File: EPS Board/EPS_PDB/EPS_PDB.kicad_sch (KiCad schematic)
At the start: 17 parts, among them J1 USB_B_Micro, J2 Conn_01x04_Pin, J3 Conn_02x26_Odd_Even, J4 Conn_02x26_Odd_Even, U1 AMS1117-3.3

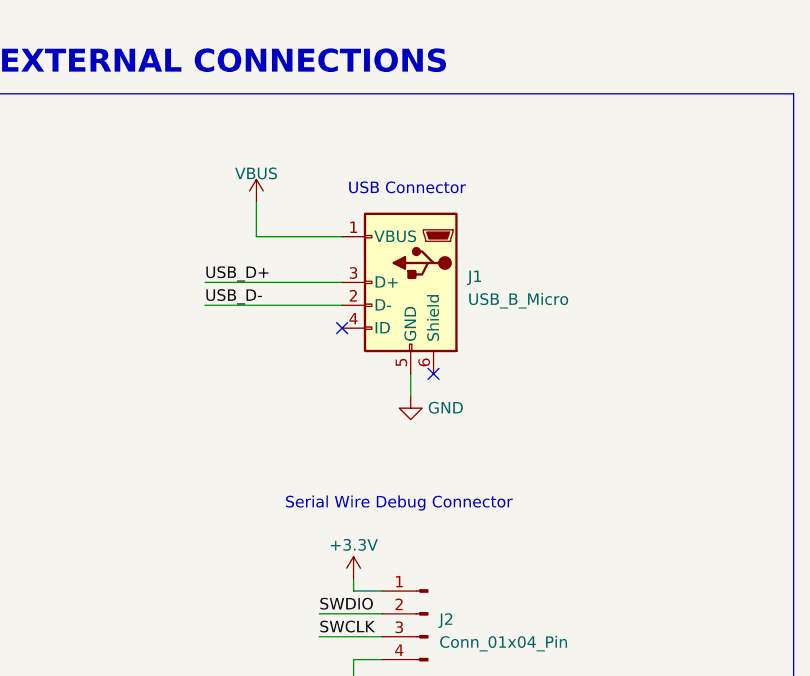
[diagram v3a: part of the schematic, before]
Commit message: texts added in schematics for clarity
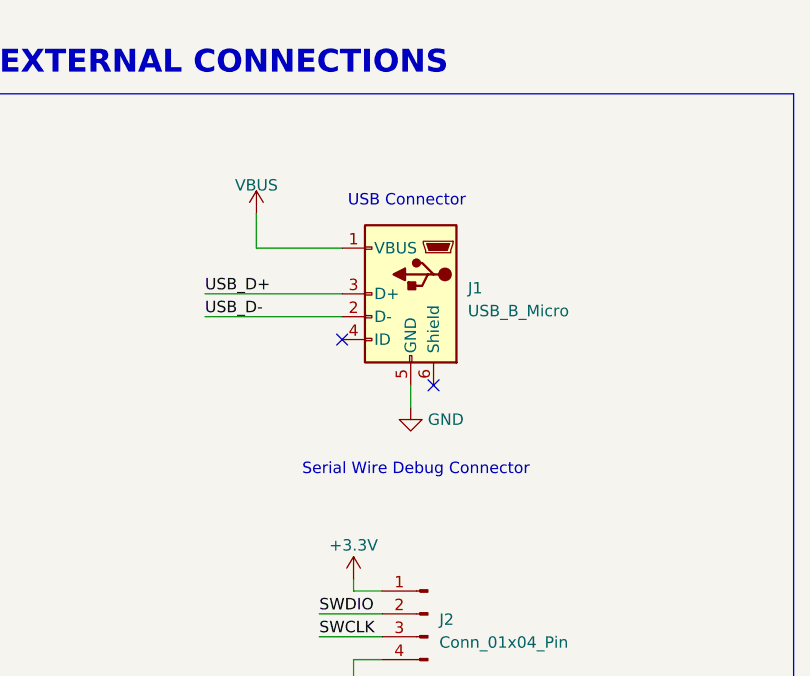
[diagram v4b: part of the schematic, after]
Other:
- moved on the sheet: J1
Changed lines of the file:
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@@
 	)
 	(no_connect
-		(at 216.535 116.84)
+		(at 216.535 118.11)
 	)
 	(no_connect
@@
 	)
 	(no_connect
-		(at 226.695 121.92)
+		(at 226.695 123.19)
 	)
 	(no_connect
@@
 	(wire
 		(pts
-			(xy 201.295 111.76) (xy 216.535 111.76)
+			(xy 201.295 113.03) (xy 216.535 113.03)
 		)
 		(stroke
@@
 	(wire
 		(pts
-			(xy 207.01 102.87) (xy 207.01 106.68)
+			(xy 207.01 104.14) (xy 207.01 107.95)
 		)
 		(stroke
@@
 	(wire
 		(pts
-			(xy 201.295 114.3) (xy 216.535 114.3)
+			(xy 201.295 115.57) (xy 216.535 115.57)
 		)
 		(stroke
@@
 	(wire
 		(pts
-			(xy 224.155 121.92) (xy 224.155 124.46)
+			(xy 224.155 123.19) (xy 224.155 125.73)
 		)
 		(stroke
@@
 	(wire
 		(pts
-			(xy 207.01 106.68) (xy 216.535 106.68)
+			(xy 207.01 107.95) (xy 216.535 107.95)
 		)
 		(stroke
@@
 	)
 	(image
-		(at 27.94 27.94)
+		(at 27.94 27.305)
 		(scale 0.0435908)
 		(data "iVBORw0KGgoAAAANSUhEUgAABeAAAAYDCAYAAACYepq1AAABhWlDQ1BJQ0MgcHJvZmlsZQAAKJF9"
@@
 	(text "USB Connector"
 		(exclude_from_sim no)
-		(at 217.17 102.235 0)
+		(at 217.17 103.505 0)
 		(effects
 			(font
@@
 	(text "Serial Wire Debug Connector"
 		(exclude_from_sim no)
-		(at 210.185 137.16 0)
+		(at 212.09 133.35 0)
 		(effects
 			(font
@@
 	)
 	(label "USB_D+"
-		(at 201.295 111.76 0)
+		(at 201.295 113.03 0)
 		(fields_autoplaced yes)
 		(effects
@@
 	)
 	(label "USB_D-"
-		(at 201.295 114.3 0)
+		(at 201.295 115.57 0)
 		(fields_autoplaced yes)
 		(effects
@@
 	(symbol
 		(lib_id "power:VBUS")
-		(at 207.01 102.87 0)
+		(at 207.01 104.14 0)
 		(unit 1)
 		(exclude_from_sim no)
@@
 		(fields_autoplaced yes)
 		(property "Reference" "#PWR02"
-			(at 207.01 106.68 0)
+			(at 207.01 107.95 0)
 			(effects
 				(font
@@
 		)
 		(property "Value" "VBUS"
-			(at 207.01 99.695 0)
+			(at 207.01 100.965 0)
 			(effects
 				(font
@@
 		)
 		(property "Footprint" ""
-			(at 207.01 102.87 0)
+			(at 207.01 104.14 0)
 			(effects
 				(font
@@
 		)
 		(property "Datasheet" ""
-			(at 207.01 102.87 0)
+			(at 207.01 104.14 0)
 			(effects
 				(font
@@
 		)
 		(property "Description" ""
-			(at 207.01 102.87 0)
+			(at 207.01 104.14 0)
 			(effects
 				(font
@@
 	(symbol
 		(lib_id "Connector:USB_B_Micro")
-		(at 224.155 111.76 0)
+		(at 224.155 113.03 0)
 		(mirror y)
 		(unit 1)
@@
 		(fields_autoplaced yes)
 		(property "Reference" "J1"
-			(at 230.505 111.125 0)
+			(at 230.505 112.395 0)
 			(effects
 				(font
@@
 		)
 		(property "Value" "USB_B_Micro"
-			(at 230.505 113.665 0)
+			(at 230.505 114.935 0)
 			(effects
 				(font
@@
 		)
 		(property "Footprint" ""
-			(at 220.345 113.03 0)
+			(at 220.345 114.3 0)
 			(effects
 				(font
@@
 		)
 		(property "Datasheet" "~"
-			(at 220.345 113.03 0)
+			(at 220.345 114.3 0)
 			(effects
 				(font
@@
 		)
 		(property "Description" ""
-			(at 224.155 111.76 0)
+			(at 224.155 113.03 0)
 			(effects
 				(font
@@
 	(symbol
 		(lib_id "power:GND")
-		(at 224.155 124.46 0)
+		(at 224.155 125.73 0)
 		(unit 1)
 		(exclude_from_sim no)
@@
 		(fields_autoplaced yes)
 		(property "Reference" "#PWR03"
-			(at 224.155 130.81 0)
+			(at 224.155 132.08 0)
 			(effects
 				(font
@@
 		)
 		(property "Value" "GND"
-			(at 226.06 125.7299 0)
+			(at 226.06 126.9999 0)
 			(effects
 				(font
@@
 		)
 		(property "Footprint" ""
-			(at 224.155 124.46 0)
+			(at 224.155 125.73 0)
 			(effects
 				(font
@@
 		)
 		(property "Datasheet" ""
-			(at 224.155 124.46 0)
+			(at 224.155 125.73 0)
 			(effects
 				(font
@@
 		)
 		(property "Description" "Power symbol creates a global label with name \"GND\" , ground"
-			(at 224.155 124.46 0)
+			(at 224.155 125.73 0)
 			(effects
 				(font

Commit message: Footprint assignment on EPS PDB Board
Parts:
- C1, C2: footprint (none) -> Capacitor_SMD:C_0805_2012Metric
- D1: footprint (none) -> LED_SMD:LED_0805_2012Metric
- H1, H2: footprint (none) -> MountingHole:MountingHole_2.2mm_M2_DIN965_Pad
- H3: renamed from H4; footprint (none) -> MountingHole:MountingHole_2.2mm_M2_DIN965_Pad
- H4: renamed from H3; footprint (none) -> MountingHole:MountingHole_2.2mm_M2_DIN965_Pad
- J1: footprint (none) -> Connector_USB:USB_Micro-AB_Molex_47590-0001
- J2: renamed from J3; footprint (none) -> PC104_BUS:SAMTEC_ESQ-126-39-G-D
- J3: renamed from J4; footprint (none) -> PC104_BUS:SAMTEC_ESQ-126-39-G-D
- J4: renamed from J2; footprint (none) -> Connector_PinHeader_2.54mm:PinHeader_1x04_P2.54mm_Horizontal
- JP1: footprint (none) -> Connector_PinHeader_2.54mm:PinHeader_1x01_P2.54mm_Vertical
- JP2: renamed from JP4; footprint (none) -> Connector_PinHeader_2.54mm:PinHeader_1x01_P2.54mm_Vertical
- R1: footprint (none) -> Resistor_SMD:R_0805_2012Metric
- TP1: footprint (none) -> TestPoint:TestPoint_Pad_D2.0mm
- TP2: footprint (none) -> TestPoint:TestPoint_Pad_2.0x2.0mm
- U1: footprint (none) -> Package_TO_SOT_SMD:SOT-223-3_TabPin2
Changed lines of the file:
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@@
 			)
 		)
-		(property "Footprint" ""
+		(property "Footprint" "Capacitor_SMD:C_0805_2012Metric"
 			(at 216.8652 215.9 0)
 			(effects
@@
 		(dnp no)
 		(fields_autoplaced yes)
-		(property "Reference" "#PWR09"
+		(property "Reference" "#PWR010"
 			(at 288.29 215.9 0)
 			(effects
@@
 			(project "EPS_PDB"
 				(path "/b6081578-ab04-44e2-a71a-4911a5b750e4"
-					(reference "#PWR09")
+					(reference "#PWR010")
 					(unit 1)
 				)
@@
 			)
 		)
-		(property "Footprint" ""
+		(property "Footprint" "LED_SMD:LED_0805_2012Metric"
 			(at 251.46 205.74 0)
 			(effects
@@
 		(dnp no)
 		(fields_autoplaced yes)
-		(property "Reference" "#PWR041"
+		(property "Reference" "#PWR07"
 			(at 318.135 201.93 0)
 			(effects
@@
 			(project "EPS_PDB"
 				(path "/b6081578-ab04-44e2-a71a-4911a5b750e4"
-					(reference "#PWR041")
+					(reference "#PWR07")
 					(unit 1)
 				)
@@
 		(dnp no)
 		(fields_autoplaced yes)
-		(property "Reference" "#PWR07"
+		(property "Reference" "#PWR09"
 			(at 184.785 207.01 0)
 			(effects
@@
 			(project "EPS_PDB"
 				(path "/b6081578-ab04-44e2-a71a-4911a5b750e4"
-					(reference "#PWR07")
+					(reference "#PWR09")
 					(unit 1)
 				)
@@
 			)
 		)
-		(property "Footprint" ""
+		(property "Footprint" "TestPoint:TestPoint_Pad_D2.0mm"
 			(at 210.82 196.85 0)
 			(effects
@@
 		(on_board yes)
 		(dnp no)
-		(property "Reference" "J3"
+		(property "Reference" "J2"
 			(at 308.61 107.315 0)
 			(effects
@@
 			)
 		)
-		(property "Footprint" ""
+		(property "Footprint" "PC104_BUS:SAMTEC_ESQ-126-39-G-D"
 			(at 307.34 144.78 0)
 			(effects
@@
 			(project "EPS_PDB"
 				(path "/b6081578-ab04-44e2-a71a-4911a5b750e4"
-					(reference "J3")
+					(reference "J2")
 					(unit 1)
 				)
@@
 		(dnp no)
 		(fields_autoplaced yes)
-		(property "Reference" "#PWR010"
+		(property "Reference" "#PWR012"
 			(at 193.04 234.315 0)
 			(effects
@@
 			(project "EPS_PDB"
 				(path "/b6081578-ab04-44e2-a71a-4911a5b750e4"
-					(reference "#PWR010")
+					(reference "#PWR012")
 					(unit 1)
 				)
@@
 		(dnp no)
 		(fields_autoplaced yes)
-		(property "Reference" "#PWR06"
+		(property "Reference" "#PWR08"
 			(at 242.57 203.835 0)
 			(effects
@@
 			(project "EPS_PDB"
 				(path "/b6081578-ab04-44e2-a71a-4911a5b750e4"
-					(reference "#PWR06")
+					(reference "#PWR08")
 					(unit 1)
 				)
@@
 			)
 		)
-		(property "Footprint" ""
+		(property "Footprint" "Connector_USB:USB_Micro-AB_Molex_47590-0001"
 			(at 220.345 114.3 0)
 			(effects
@@
 		(on_board yes)
 		(dnp no)
-		(property "Reference" "J4"
+		(property "Reference" "J3"
 			(at 358.14 107.95 0)
 			(effects
@@
 			)
 		)
-		(property "Footprint" ""
+		(property "Footprint" "PC104_BUS:SAMTEC_ESQ-126-39-G-D"
 			(at 356.87 144.78 0)
 			(effects
@@
 			(project "EPS_PDB"
 				(path "/b6081578-ab04-44e2-a71a-4911a5b750e4"
-					(reference "J4")
+					(reference "J3")
 					(unit 1)
 				)
@@
 			)
 		)
-		(property "Footprint" ""
+		(property "Footprint" "MountingHole:MountingHole_2.2mm_M2_DIN965_Pad"
 			(at 382.27 64.135 0)
 			(effects
@@
 			)
 		)
-		(property "Footprint" ""
+		(property "Footprint" "Capacitor_SMD:C_0805_2012Metric"
 			(at 194.0052 215.265 0)
 			(effects
@@
 		(on_board yes)
 		(dnp no)
-		(property "Reference" "JP4"
+		(property "Reference" "JP2"
 			(at 371.475 201.93 0)
 			(effects
@@
 			)
 		)
-		(property "Footprint" ""
+		(property "Footprint" "Connector_PinHeader_2.54mm:PinHeader_1x01_P2.54mm_Vertical"
 			(at 371.475 205.74 0)
 			(effects
@@
 			(project ""
 				(path "/b6081578-ab04-44e2-a71a-4911a5b750e4"
-					(reference "JP4")
+					(reference "JP2")
 					(unit 1)
 				)
@@
 		(dnp no)
 		(fields_autoplaced yes)
-		(property "Reference" "J2"
+		(property "Reference" "J4"
 			(at 227.33 149.225 0)
 			(effects
@@
 			)
 		)
-		(property "Footprint" ""
+		(property "Footprint" "Connector_PinHeader_2.54mm:PinHeader_1x04_P2.54mm_Horizontal"
 			(at 226.06 148.59 0)
 			(effects
@@
 			(project "EPS_PDB"
 				(path "/b6081578-ab04-44e2-a71a-4911a5b750e4"
-					(reference "J2")
+					(reference "J4")
 					(unit 1)
 				)
@@
 			)
 		)
-		(property "Footprint" ""
+		(property "Footprint" "MountingHole:MountingHole_2.2mm_M2_DIN965_Pad"
 			(at 354.33 64.135 0)
 			(effects
@@
 		(on_board yes)
 		(dnp no)
-		(property "Reference" "H3"
+		(property "Reference" "H4"
 			(at 384.175 71.12 90)
 			(effects
@@
 			)
 		)
-		(property "Footprint" ""
+		(property "Footprint" "MountingHole:MountingHole_2.2mm_M2_DIN965_Pad"
 			(at 382.905 76.835 0)
 			(effects
@@
 			(project "EPS_PDB"
 				(path "/b6081578-ab04-44e2-a71a-4911a5b750e4"
-					(reference "H3")
+					(reference "H4")
 					(unit 1)
 				)
@@
 		(dnp no)
 		(fields_autoplaced yes)
-		(property "Reference" "#PWR042"
+		(property "Reference" "#PWR011"
 			(at 318.135 215.9 0)
 			(effects
@@
 			(project "EPS_PDB"
 				(path "/b6081578-ab04-44e2-a71a-4911a5b750e4"
-					(reference "#PWR042")
+					(reference "#PWR011")
 					(unit 1)
 				)
@@
 			)
 		)
-		(property "Footprint" ""
+		(property "Footprint" "Connector_PinHeader_2.54mm:PinHeader_1x01_P2.54mm_Vertical"
 			(at 227.965 205.74 0)
 			(effects
@@
 			)
 		)
-		(property "Footprint" ""
+		(property "Footprint" "TestPoint:TestPoint_Pad_2.0x2.0mm"
 			(at 240.03 224.79 0)
 			(effects
@@
 			)
 		)
-		(property "Footprint" ""
+		(property "Footprint" "Resistor_SMD:R_0805_2012Metric"
 			(at 262.763 220.345 90)
 			(effects
@@
 			)
 		)
-		(property "Footprint" ""
+		(property "Footprint" "Package_TO_SOT_SMD:SOT-223-3_TabPin2"
 			(at 206.375 200.66 0)
 			(effects
@@
 		(dnp no)
 		(fields_autoplaced yes)
-		(property "Reference" "#PWR08"
+		(property "Reference" "#PWR06"
 			(at 288.29 201.93 0)
 			(effects
@@
 			(project "EPS_PDB"
 				(path "/b6081578-ab04-44e2-a71a-4911a5b750e4"
-					(reference "#PWR08")
+					(reference "#PWR06")
 					(unit 1)
 				)
@@
 		(on_board yes)
 		(dnp no)
-		(property "Reference" "H4"
+		(property "Reference" "H3"
 			(at 353.06 71.12 90)
 			(effects
@@
 			)
 		)
-		(property "Footprint" ""
+		(property "Footprint" "MountingHole:MountingHole_2.2mm_M2_DIN965_Pad"
 			(at 354.33 76.835 0)
 			(effects
@@
 			(project "EPS_PDB"
 				(path "/b6081578-ab04-44e2-a71a-4911a5b750e4"
-					(reference "H4")
-					(unit 1)
-				)
+					(reference "H3")
+					(unit 1)
+				)
